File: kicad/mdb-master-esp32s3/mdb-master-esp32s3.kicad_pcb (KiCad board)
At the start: 2 copper layers, 41.8 x 50.2 mm, 40 parts, among them J2 MDB_Connector, J3 Barrel_Jack, J5 Conn_02x10_Odd_Even, P1 USB_C_Plug_USB2.0, Q1 BC807, U2 LM317_SOT-223, Y1 Crystal

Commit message: Refacting kicad pcb
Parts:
- removed +3v3, gnd, vin: TestPoint, TestPoint:TestPoint_Pad_D1.0mm
- removed B: Boot, Button_Switch_SMD:SW_Tactile_SPST_NO_Straight_CK_PTS636Sx25SMTRLFS
- removed BZ1: Buzzer, Buzzer_Beeper:Buzzer_12x9.5RM7.6
- removed C3: C, Capacitor_SMD:C_0603_1608Metric
- removed D2: LED, LED_SMD:LED_0603_1608Metric
- removed ESP32-S3: ESP32-S3, Package_DFN_QFN:QFN-56-1EP_7x7mm_P0.4mm_EP5.6x5.6mm
- removed J5: Conn_02x10_Odd_Even, Connector_PinHeader_2.54mm:PinHeader_2x10_P2.54mm_Vertical
- removed P1: USB_C_Plug_USB2.0, Connector_USB:USB_C_Receptacle_G-Switch_GT-USB-7010ASV
- removed R: Reset, Button_Switch_SMD:SW_Tactile_SPST_NO_Straight_CK_PTS636Sx25SMTRLFS
- removed R15, R16, R17: R, Resistor_SMD:R_0603_1608Metric
- added 0: SW_Push, Button_Switch_SMD:SW_Tactile_SPST_NO_Straight_CK_PTS636Sx25SMTRLFS, F.Cu at (131.1, 117.5)
- added 21: LED, LED_SMD:LED_0603_1608Metric, F.Cu at (164.1, 94.1)
- added J1: MDB_Connector, Connector_Molex:Molex_Mini-Fit_Jr_5566-06A_2x03_P4.20mm_Vertical, F.Cu at (163.3, 79.6)
- added J4: Conn_02x11_Odd_Even, Connector_PinHeader_2.54mm:PinHeader_2x11_P2.54mm_Vertical, F.Cu at (129.9, 86.0)
- added U1: ESP32-S3R8, Package_DFN_QFN:QFN-56-1EP_7x7mm_P0.4mm_EP5.6x5.6mm, F.Cu at (147.5, 103.3)
- added reset: TestPoint, TestPoint:TestPoint_Pad_D1.0mm, F.Cu at (142.1, 95.3)
- AE1: footprint RF_Antenna:Texas_SWRA117D_2.4GHz_Right -> RF_Antenna:Texas_SWRA117D_2.4GHz_Left
- C4: value C -> 1.8pf
- C5, C6: value C -> 22pf
- C7: value C_Polarized -> 22pf; footprint Capacitor_Tantalum_SMD:CP_EIA-3216-18_Kemet-A -> Capacitor_SMD:C_0603_1608Metric
- D1: value LED -> 1N5819HWQ; footprint LED_SMD:LED_0603_1608Metric -> Diode_SMD:D_SOD-123
- D3: value D -> LED; footprint Diode_SMD:D_SOD-123 -> LED_SMD:LED_0603_1608Metric
- J2: value MDB_Connector -> Barrel_Jack; footprint Connector_Molex:Molex_Mini-Fit_Jr_5566-06A_2x03_P4.20mm_Vertical -> Connector_BarrelJack:BarrelJack_Horizontal
- J3: value Barrel_Jack -> USB_C_Receptacle_USB2.0_16P; footprint Connector_BarrelJack:BarrelJack_Horizontal -> Connector_USB:USB_C_Receptacle_G-Switch_GT-USB-7010ASV
- L1: value 47nH -> 2.4nh
- R1, R3, R4, R5, R6, R7, R9: value R -> 3.3k
- R10, R11: value R -> 240ohm
- R2: value R -> 180ohm
- R8: value 240 -> 3.3k
- U2: value LM317_SOT-223 -> AMS1117-3.3; footprint Package_TO_SOT_SMD:SOT-223-3_TabPin2 -> Package_TO_SOT_SMD:SOT-223
- Y1: value Crystal -> 40000hz
- moved R10 51.9 mm to (159.8, 94.1)
- moved R11 46.9 mm to (159.8, 96.5)
- moved D3 44.2 mm to (164.1, 96.5), turned to 180 degrees
- moved R2 36.9 mm to (149.5, 79.5), turned to -90 degrees
- moved C6 36.2 mm to (142.4, 92.1), turned to 0 degrees
- moved R1 33.5 mm to (152.4, 79.5), turned to 90 degrees
- moved R5 31.6 mm to (143.2, 79.5), turned to 90 degrees
- moved R7 31.4 mm to (148.8, 95.3), turned to 0 degrees
- moved C4 26.0 mm to (136.3, 82.9), turned to 180 degrees
- moved R3 25.6 mm to (138.8, 100.4)
- moved C7 25.1 mm to (155.8, 101.2)
- moved R6 22.4 mm to (152.6, 94.1)
- moved U2 21.1 mm to (161.7, 103.4)
- moved C2 20.4 mm to (144.1, 110.2), turned to -90 degrees
- moved J3 20.2 mm to (144.8, 117.5), turned to 0 degrees
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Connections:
- C1 pad 1: Net-(AE1-A) -> GND
- C1 pad 2: Net-(U1-LNA_IN/RF) -> +3V3
- C2 pad 1: GND -> +3V3
- C2 pad 2: +3V3 -> GND
- C4 pad 1: GND -> Net-(AE1-A)
- C4 pad 2: Net-(U1-XTAL_N) -> Net-(U1-LNA_IN/RF)
- C5 pad 2: Net-(U1-XTAL_P) -> Net-(U1-XTAL_N)
- C6 pad 2: +3V3 -> Net-(U1-XTAL_P)
- C7 pad 1: +3V3 -> GND
- C7 pad 2: GND -> +3V3
- D1 pad 1: Net-(D1-K) -> /vin
- D1 pad 2: /io21 -> Net-(D1-A)
- D3 pad 1: /vin -> GND
- J2 pad 3: unconnected-(J2-Pin_3-Pad3) -> (no net)
- L1 pad 1: Net-(AE1-A) -> GND
- L1 pad 2: GND -> Net-(AE1-A)
- R1 pad 2: Net-(U1-CHIP_PU/RESET) (its old number) -> /io4
- R10 pad 2: GND -> /io21
- R11 pad 1: Net-(P1-CC) -> Net-(D3-A)
- R11 pad 2: GND -> +3V3
- R2 pad 1: GND -> /mdb_master_transmit
- R2 pad 2: Net-(D1-K) -> GND
- R3 pad 1: GND -> +3V3
- R4 pad 1: Net-(U1-GPIO46) -> /boot
- R4 pad 2: GND -> +3V3
- R5 pad 1: Net-(U1-GPIO45) -> /io5
- R5 pad 2: GND -> Net-(Q1-B)
- R6 pad 1: /boot -> Net-(U1-GPIO45)
- R6 pad 2: +3V3 -> GND
- R7 pad 1: Net-(U2-ADJ) -> Net-(U1-GPIO46)
- R8 pad 1: +3V3 -> Net-(J3-CC2)
- R8 pad 2: Net-(U2-ADJ) -> GND
- R9 pad 1: Net-(P1-SHIELD) -> Net-(J3-CC1)
- U2 pad 1: Net-(U2-ADJ) -> GND
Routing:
- net GND: track 230.0 -> 170.5 mm
- net Net-(U1-CHIP_PU/RESET) (its old number): track 47.9 -> 0.00 mm, vias 2 -> 0
- net +3V3: track 133.5 -> 95.9 mm, vias 8 -> 7
- net Net-(P1-SHIELD): track 20.4 -> 0.00 mm
- net /boot: track 49.7 -> 34.1 mm
- net /io2: track 13.7 -> 28.0 mm
- net Net-(D3-A): track 16.6 -> 2.70 mm, vias 2 -> 0
- net /io9: track 11.4 -> 25.0 mm
- net Net-(D1-A): track 0.00 -> 13.6 mm, vias 0 -> 2
- net /io8: track 13.8 -> 27.1 mm
- net /io21: track 33.4 -> 45.9 mm
- net /io12: track 9.55 -> 21.4 mm
- net /io11: track 11.2 -> 22.8 mm
- net Net-(J3-CC2): track 0.00 -> 11.4 mm
- net /io5: track 59.7 -> 48.4 mm, vias 3 -> 2
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- removed copper zone on F.Cu, net GND
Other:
- board size 41.8 x 50.2 mm -> 41 x 46 mm
- board text added: "+3v3"
- board text added: "0"
- board text added: "01"
- board text added: "02"
- board text added: "04"
- board text added: "05"
- board text added: "06"
- board text added: "07"
- board text added: "08"
- board text added: "09"
- board text added: "10"
- board text added: "11"
- board text added: "12"
- board text added: "13"
- board text added: "14"
- board text added: "17"
- board text added: "18"
- board text added: "21"
- board text added: "gnd"
- board text added: "rx"
- board text added: "tx"
- board text added: "vin"
- board text removed: "7 gnd 8 gnd 9 tx 10 rx 11 1 12 2 13 4 14 5 +3v3 17 vin 18"

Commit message: Refacting kicad pcb
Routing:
- net /io21: track 45.9 -> 42.4 mm
- net GND: track 170.5 -> 171.5 mm, vias 5 -> 4
- net Net-(D1-A): track 13.6 -> 14.3 mm

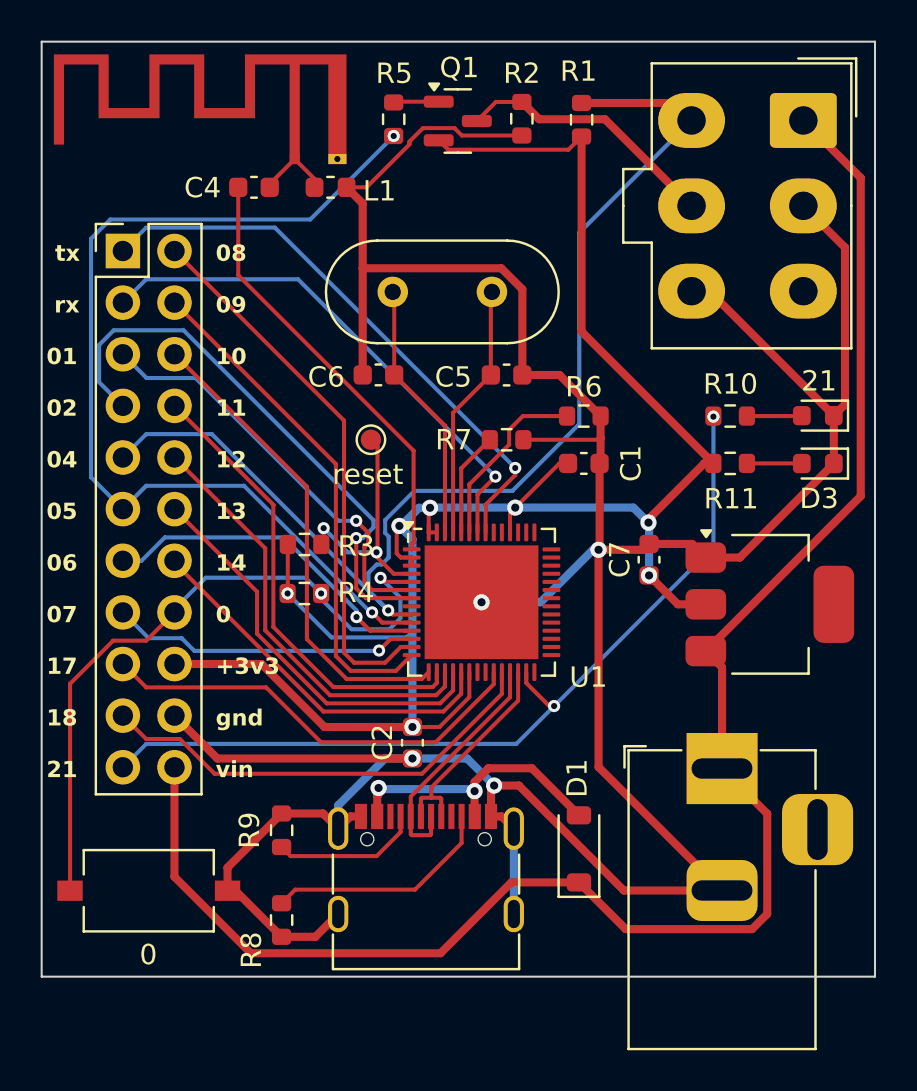
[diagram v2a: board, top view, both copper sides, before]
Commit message: Refacting Kicad layout
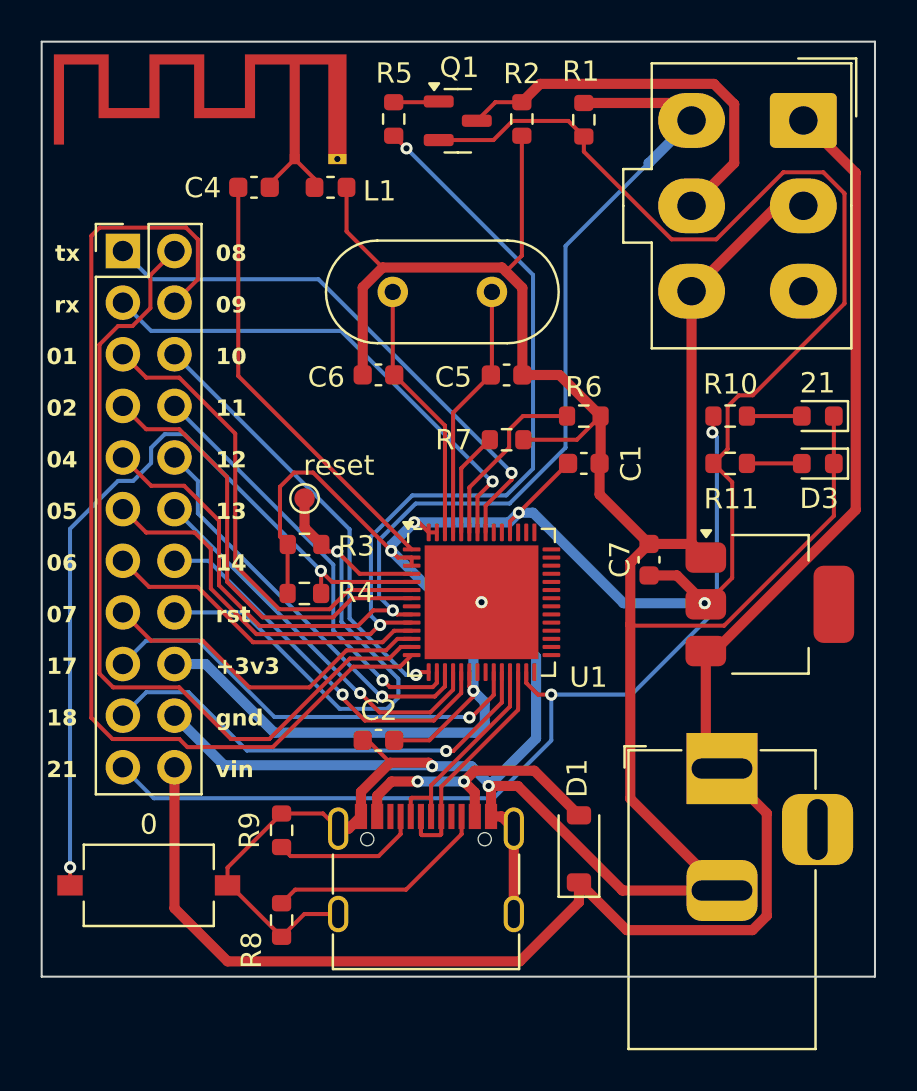
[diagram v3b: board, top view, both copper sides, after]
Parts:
- moved reset 4.36 mm to (138.8, 98.2)
- moved C2 1.68 mm to (142.4, 110.1), turned to 180 degrees
- moved 0 0.27 mm to (131.1, 117.2)
- moved R1 0.11 mm to (152.6, 79.5)
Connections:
- J4 pad 16: /boot -> /reset
- R3 pad 2: Net-(U1-CHIP_PU/RESET) -> /reset
- U1 pad 28: unconnected-(U1-SPI_CS1/GPIO26-Pad28) -> /spics1
- U1 pad 4: Net-(U1-CHIP_PU/RESET) -> /reset
- reset pad 1: Net-(U1-CHIP_PU/RESET) -> /reset
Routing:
- net /reset: track 0.00 -> 29.3 mm, vias 0 -> 1
- net +3V3: track 96.1 -> 124.3 mm, vias 7 -> 5
- net /io9: track 25.0 -> 51.2 mm
- net /io8: track 27.1 -> 41.3 mm
- net Net-(U1-CHIP_PU/RESET): track 11.9 -> 0.00 mm, vias 2 -> 0
- net /boot: track 34.1 -> 40.8 mm
- net /mdb_master_transmit: track 13.1 -> 19.7 mm
- net /io2: track 28.0 -> 21.9 mm, vias 1 -> 0
- net GND: track 171.5 -> 177.5 mm, vias 4 -> 3
- net /io21: track 42.4 -> 46.7 mm
- net /io1: track 20.7 -> 23.6 mm, vias 1 -> 0
- net /io5: track 48.4 -> 51.3 mm
- net /io10: track 23.7 -> 21.7 mm, vias 0 -> 1
- net /vin: track 83.4 -> 85.4 mm
- net /io11: track 22.8 -> 21.2 mm, vias 0 -> 1
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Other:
- board text added: "rst"
- board text removed: "0"

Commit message: Refacting PCB
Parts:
- removed reset: TestPoint, TestPoint:TestPoint_Pad_D1.0mm
- moved R10 0.40 mm to (160.2, 94.1)
- moved R11 0.40 mm to (160.2, 96.5)
- moved D3 0.11 mm to (163.9, 96.5)
- moved 21 0.11 mm to (163.9, 94.1)
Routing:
- net +3V3: track 124.3 -> 119.7 mm
- net /reset: track 29.3 -> 26.5 mm
- net Net-(D2-A): track 2.70 -> 2.19 mm

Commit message: Sending gerber files to pcbway
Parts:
- moved C1 0.75 mm to (152.6, 97.2), turned to -90 degrees
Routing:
- net /io8: track 41.3 -> 39.2 mm
- net GND: track 177.4 -> 179.2 mm
- net /io7: track 16.7 -> 15.2 mm
- net +3V3: track 119.7 -> 120.4 mm

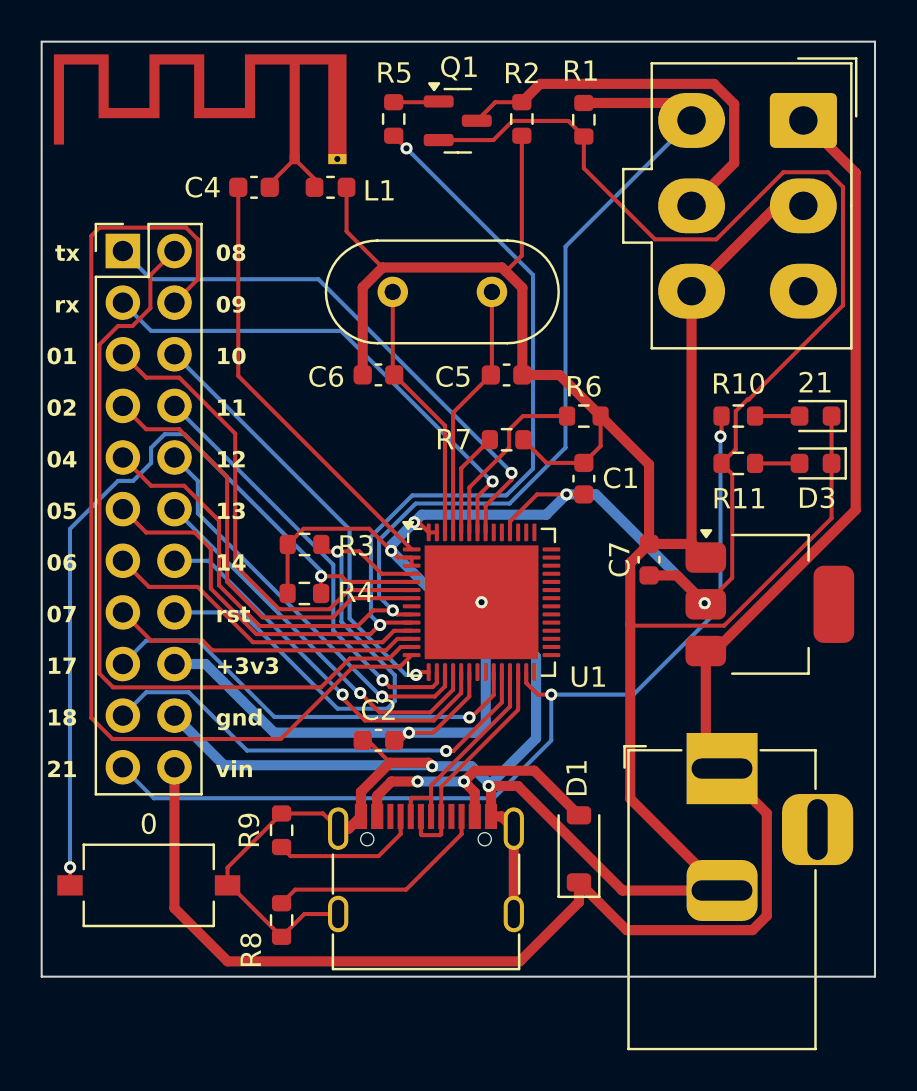
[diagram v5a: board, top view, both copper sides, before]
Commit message: Refacting kicad layout
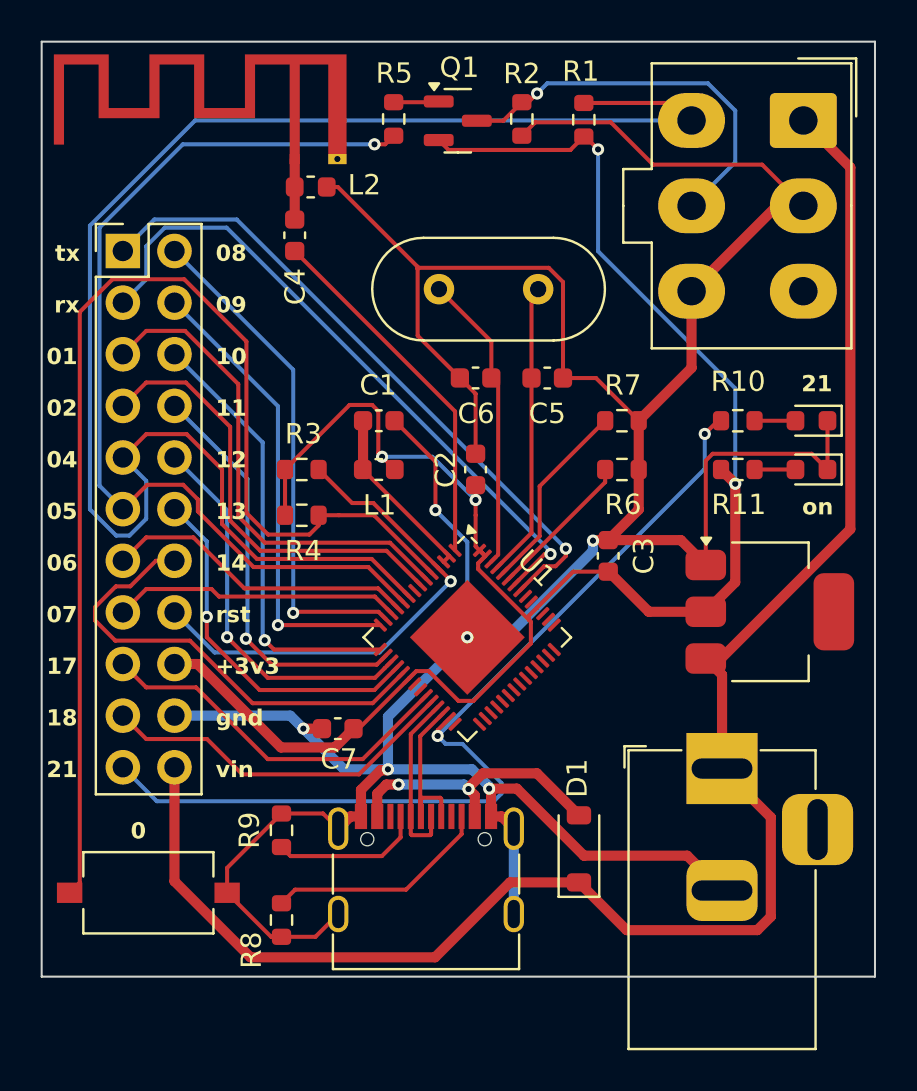
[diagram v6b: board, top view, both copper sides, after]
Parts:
- removed 0: SW_Push, Button_Switch_SMD:SW_Tactile_SPST_NO_Straight_CK_PTS636Sx25SMTRLFS
- removed 21: LED, LED_SMD:LED_0603_1608Metric
- added C3: 10uF, Capacitor_SMD:C_0603_1608Metric, F.Cu at (153.8, 101.0)
- added D2: LED, LED_SMD:LED_0603_1608Metric, F.Cu at (163.8, 94.3)
- added L2: 2.4nh, Inductor_SMD:L_0603_1608Metric, F.Cu at (139.1, 82.8)
- added SW1: SW_Push, Button_Switch_SMD:SW_Tactile_SPST_NO_Straight_CK_PTS636Sx25SMTRLFS, F.Cu at (131.1, 117.6)
- C1: value C -> 0.1uF
- C2: value C -> 1uF
- C7: value 22pf -> 1uF
- L1: value 2.4nh -> 2nH
- U1: footprint Package_DFN_QFN:QFN-56-1EP_7x7mm_P0.4mm_EP5.6x5.6mm -> Package_DFN_QFN:QFN-56-1EP_7x7mm_P0.4mm_EP4x4mm
- moved C7 17.4 mm to (140.4, 109.5), turned to 0 degrees
- moved C2 14.2 mm to (147.2, 96.8), turned to -90 degrees
- moved L1 14.1 mm to (142.5, 96.8)
- moved C1 10.5 mm to (142.5, 94.3), turned to 0 degrees
- moved R7 5.75 mm to (154.4, 94.3)
- moved C6 4.78 mm to (147.2, 92.2)
- moved R4 3.85 mm to (138.7, 99.0)
- moved R3 3.69 mm to (138.7, 96.8)
- moved R6 3.23 mm to (154.4, 96.8)
- moved C4 3.09 mm to (138.3, 85.2), turned to -90 degrees
- moved Y1 2.28 mm to (145.4, 87.9)
- moved C5 2.01 mm to (150.8, 92.2)
- moved U1 1.86 mm to (146.8, 105.0), turned to -45 degrees
- moved U2 0.37 mm to (161.7, 103.8)
- moved D3 0.36 mm to (163.8, 96.8)
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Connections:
- C1 pad 1: GND -> VDD3P3
- C1 pad 2: +3V3 -> GND
- C2 pad 1: +3V3 -> GND
- C2 pad 2: GND -> +3V3
- L1 pad 1: GND -> +3V3
- L1 pad 2: Net-(AE1-A) -> VDD3P3
- U1 pad 2: +3V3 -> VDD3P3
- U1 pad 3: +3V3 -> VDD3P3
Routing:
- net /io9: track 50.9 -> 23.0 mm, vias 0 -> 1
- net +3V3: track 120.4 -> 95.7 mm, vias 5 -> 4
- net /io4: track 59.0 -> 77.9 mm, vias 1 -> 0
- net /boot: track 40.7 -> 58.8 mm, vias 2 -> 0
- net /io8: track 39.2 -> 25.0 mm, vias 0 -> 1
- net VDD3P3: track 0.00 -> 8.90 mm
- net /u0rxd: track 24.7 -> 32.7 mm
- net /u0txd: track 27.1 -> 32.5 mm
- net /io18: track 22.8 -> 17.9 mm, vias 1 -> 0
- net Net-(U1-GPIO46): track 5.14 -> 9.60 mm
- net /io14: track 19.1 -> 23.0 mm, vias 1 -> 0
- net /io17: track 21.9 -> 18.2 mm, vias 1 -> 0
- net /io5: track 51.3 -> 47.7 mm, vias 2 -> 1
- net Net-(U1-LNA_IN/RF): track 21.3 -> 18.0 mm
- net /usb+: track 11.4 -> 8.37 mm
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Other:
- board text added: "0"
- board text added: "on"
